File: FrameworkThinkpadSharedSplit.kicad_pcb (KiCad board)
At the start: 2 copper layers, 298.1 x 158.9 mm, 171 parts, among them J1 Conn_01x05_Socket, J10 Conn_01x06_Socket, J11 Conn_01x06_Socket, J12 Conn_01x06_Socket, J2 Conn_01x05_Socket, J3 Conn_01x05_Socket, J4 Conn_01x07_Socket, J5 Conn_01x07_Socket, J6 Conn_01x07_Socket, J7 Conn_01x07_Socket, J8 Conn_01x05_Socket, U1 RP2040_Pro_Micro, U2 Arduino_Pro_Micro

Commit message: added missing row and pullup resistors
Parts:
- removed D36, D37, D38, D39: Diode, ScottoKeebs_Components:Diode_SOD-123
- removed J1, J2, J3, J8: Conn_01x05_Socket, Connector_Molex:Molex_PicoBlade_53048-0510_1x05_P1.25mm_Horizontal
- removed S36, S37, S38, S39: Keyswitch, ScottoKeebs_Choc:Choc_V1V2_1.00u
- added D29: Diode, ScottoKeebs_Components:Diode_SOD-123, B.Cu at (51.0, 179.7)
- added D30: Diode, ScottoKeebs_Components:Diode_SOD-123, B.Cu at (70.0, 179.7)
- added D31: Diode, ScottoKeebs_Components:Diode_SOD-123, B.Cu at (89.0, 179.7)
- added D32: Diode, ScottoKeebs_Components:Diode_SOD-123, B.Cu at (107.0, 179.7)
- added D67: Diode, ScottoKeebs_Components:Diode_SOD-123, B.Cu at (255.0, 162.3)
- added D68: Diode, ScottoKeebs_Components:Diode_SOD-123, B.Cu at (274.0, 162.3)
- added D69: Diode, ScottoKeebs_Components:Diode_SOD-123, B.Cu at (292.0, 162.7)
- added D70: Diode, ScottoKeebs_Components:Diode_SOD-123, B.Cu at (311.0, 162.3)
- added D71: Diode, ScottoKeebs_Components:Diode_SOD-123, B.Cu at (199.0, 179.7)
- added D72: Diode, ScottoKeebs_Components:Diode_SOD-123, B.Cu at (218.0, 179.7)
- added D73: Diode, ScottoKeebs_Components:Diode_SOD-123, B.Cu at (236.0, 179.7)
- added D74: Diode, ScottoKeebs_Components:Diode_SOD-123, B.Cu at (255.0, 179.7)
- added D75: Diode, ScottoKeebs_Components:Diode_SOD-123, B.Cu at (273.0, 179.7)
- added D76: Diode, ScottoKeebs_Components:Diode_SOD-123, B.Cu at (292.0, 179.7)
- added D78: Diode, ScottoKeebs_Components:Diode_SOD-123, B.Cu at (311.0, 179.7)
- added D79: Diode, ScottoKeebs_Components:Diode_SOD-123, B.Cu at (199.0, 197.7)
- added D80: Diode, ScottoKeebs_Components:Diode_SOD-123, B.Cu at (218.0, 197.3)
- added D81: Diode, ScottoKeebs_Components:Diode_SOD-123, B.Cu at (236.0, 197.3)
- added J13: Conn_01x06_Socket, Connector_Molex:Molex_PicoBlade_53048-0610_1x06_P1.25mm_Horizontal, B.Cu at (29.0, 125.0)
- added J14: Conn_01x06_Socket, Connector_Molex:Molex_PicoBlade_53048-0610_1x06_P1.25mm_Horizontal, B.Cu at (167.3, 126.9)
- added J15: Conn_01x06_Socket, Connector_Molex:Molex_PicoBlade_53048-0610_1x06_P1.25mm_Horizontal, B.Cu at (179.0, 133.2)
- added J9: Conn_01x06_Socket, Connector_Molex:Molex_PicoBlade_53048-0610_1x06_P1.25mm_Horizontal, F.Cu at (36.0, 84.3)
- added R6: Resistor 4.7k, ScottoKeebs_Components:Resistor_1206, F.Cu at (36.5, 65.0)
- added R7: Resistor 4.7k, ScottoKeebs_Components:Resistor_1206, F.Cu at (44.0, 65.0)
- added S29: Keyswitch, ScottoKeebs_Choc:Choc_V1V2_1.00u, F.Cu at (43.0, 181.9)
- added S30: Keyswitch, ScottoKeebs_Choc:Choc_V1V2_1.00u, F.Cu at (61.6, 181.9)
- added S31: Keyswitch, ScottoKeebs_Choc:Choc_V1V2_1.00u, F.Cu at (80.2, 181.9)
- added S32: Keyswitch, ScottoKeebs_Choc:Choc_V1V2_1.00u, F.Cu at (98.8, 181.9)
- added S67: Keyswitch, ScottoKeebs_Choc:Choc_V1V2_1.00u, F.Cu at (246.5, 164.3)
- added S68: Keyswitch, ScottoKeebs_Choc:Choc_V1V2_1.00u, F.Cu at (265.1, 164.3)
- added S69: Keyswitch, ScottoKeebs_Choc:Choc_V1V2_1.00u, F.Cu at (283.7, 164.3)
- added S70: Keyswitch, ScottoKeebs_Choc:Choc_V1V2_1.00u, F.Cu at (302.3, 164.3)
- added S71: Keyswitch, ScottoKeebs_Choc:Choc_V1V2_1.00u, F.Cu at (190.7, 181.9)
- added S72: Keyswitch, ScottoKeebs_Choc:Choc_V1V2_1.00u, F.Cu at (209.3, 181.9)
- added S73: Keyswitch, ScottoKeebs_Choc:Choc_V1V2_1.00u, F.Cu at (227.9, 181.9)
- added S74: Keyswitch, ScottoKeebs_Choc:Choc_V1V2_1.00u, F.Cu at (246.5, 181.9)
- added S75: Keyswitch, ScottoKeebs_Choc:Choc_V1V2_1.00u, F.Cu at (265.1, 181.9)
- added S76: Keyswitch, ScottoKeebs_Choc:Choc_V1V2_1.00u, F.Cu at (283.7, 181.9)
- added S77: Keyswitch, ScottoKeebs_Choc:Choc_V1V2_1.00u, F.Cu at (302.3, 181.9)
- added S78: Keyswitch, ScottoKeebs_Choc:Choc_V1V2_1.00u, F.Cu at (190.7, 199.5)
- added S79: Keyswitch, ScottoKeebs_Choc:Choc_V1V2_1.00u, F.Cu at (209.3, 199.5)
- added S80: Keyswitch, ScottoKeebs_Choc:Choc_V1V2_1.00u, F.Cu at (227.9, 199.5)
- moved D40 172.6 mm to (126.0, 197.7)
- moved D42 172.3 mm to (163.0, 197.0)
- moved S40 171.9 mm to (117.5, 199.5)
- moved S41 171.9 mm to (136.1, 199.5)
- moved S42 171.9 mm to (154.7, 199.5)
- moved D41 171.4 mm to (145.0, 197.0)
- moved J4 41.9 mm to (89.2, 84.1)
- moved J6 36.9 mm to (49.5, 84.0)
- moved REF** 23.5 mm to (311.0, 204.0)
- moved REF** 23.5 mm to (34.0, 204.0)
- moved D65 18.6 mm to (218.0, 161.7)
- moved D43 18.2 mm to (199.0, 109.0)
- moved D50 18.2 mm to (199.0, 127.0)
- moved D53 18.2 mm to (255.0, 127.0)
- moved D56 18.2 mm to (311.0, 127.0)
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- renumbered D29 to D82, D30 to D83, D31 to D84, D32 to D85, D67 to D86
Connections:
- S40 pad 1: Net-(J5-Pin_5) -> Net-(J7-Pin_5)
- S41 pad 1: Net-(J5-Pin_6) -> Net-(J7-Pin_6)
- S42 pad 1: Net-(J5-Pin_7) -> Net-(J7-Pin_7)
- U1 pad 10: Col 4 -> Col 10
- U1 pad 11: Col 5 -> Col 11
- U1 pad 12: Col 6 -> Col 12
- U1 pad 13: Col 7 -> Col 13
- U1 pad 14: Col 8 -> Caps Led
- U1 pad 15: Col 9 -> Row 5
- U1 pad 16: Col 10 -> Row 4
- U1 pad 17: Col 11 -> Row 3
- U1 pad 18: Col 12 -> Row 2
- U1 pad 19: Numpad Led -> Row 1
- U1 pad 2: Col 0 -> Trackpoint Data
- U1 pad 20: Caps Led -> Row 0
- U1 pad 21: Row 4 -> Col 1
- U1 pad 22: Row 3 -> Col 2
- U1 pad 23: Row 2 -> Col 3
- U1 pad 24: Row 1 -> Col 4
- U1 pad 25: Row 0 -> Col 5
- U1 pad 26: Col 13 -> Col 6
- U1 pad 29: Trackpoint GND -> unconnected-(U1-GND-Pad29)
- U1 pad 3: Col 1 -> Trackpoint Clock
- U1 pad 30: LED PWR -> unconnected-(U1-5v-Pad30)
- U1 pad 31: unconnected-(U1-GP11-Pad31) -> Col 0
- U1 pad 4: Power LED GND -> Trackpoint GND
- U1 pad 5: unconnected-(U1-GND-Pad5) -> Power LED GND
- U1 pad 6: Col 2 -> Numpad Led
- U1 pad 7: Col 3 -> Col 7
- U1 pad 8: Trackpoint Data -> Col 8
- U1 pad 9: Trackpoint Clock -> Col 9
- U2 pad 21: unconnected-(U2-VCC-Pad21) -> LED PWR
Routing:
- net Net-(D71-K): track 0.00 -> 203.9 mm, vias 0 -> 2
- net Net-(D79-K): track 0.00 -> 136.0 mm, vias 0 -> 2
- net Net-(D40-K): track 159.8 -> 275.1 mm
- net Trackpoint Data: track 0.00 -> 94.3 mm, vias 0 -> 3
- net Trackpoint GND: track 0.00 -> 87.1 mm, vias 0 -> 2
- net Trackpoint Clock: track 0.00 -> 86.2 mm, vias 0 -> 3
- net Net-(D64-K): track 124.9 -> 188.4 mm, vias 0 -> 2
- net Net-(J11-Pin_6): track 0.00 -> 59.5 mm
- net Trackpoint PWR: track 0.00 -> 57.4 mm, vias 0 -> 1
- net Net-(J11-Pin_5): track 0.00 -> 57.4 mm
- net Net-(J11-Pin_4): track 0.00 -> 54.3 mm
- net Col 7: track 75.9 -> 21.7 mm, vias 2 -> 0
- net Row 5: track 0.00 -> 53.5 mm
- net Net-(J11-Pin_3): track 0.00 -> 50.8 mm
- net LED PWR: track 77.1 -> 26.4 mm
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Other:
- board size 298.1 x 158.9 mm -> 298.1 x 174.5 mm

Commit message: shrunk pcb down on the top and bottom
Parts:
- moved J7 26.2 mm to (29.4, 122.5), turned to 90 degrees
- moved J5 24.9 mm to (179.0, 122.3), turned to 90 degrees
- moved J12 9.60 mm to (257.7, 92.9)
- moved J4 9.60 mm to (89.2, 93.7)
- moved J9 9.60 mm to (36.0, 93.9)
- moved R1 9.60 mm to (276.8, 92.6)
- moved R2 9.60 mm to (285.3, 96.1)
- moved R3 9.60 mm to (293.1, 92.6)
- moved R4 9.60 mm to (300.8, 96.1)
- moved R5 9.60 mm to (309.8, 93.1)
- moved REF** 9.60 mm to (316.8, 93.1)
- moved REF** 9.60 mm to (243.8, 93.1)
- moved J10 9.60 mm to (106.1, 64.5)
- moved J11 9.60 mm to (88.9, 52.9)
- moved REF** 9.60 mm to (28.5, 50.9)
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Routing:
- net Net-(J7-Pin_7): track 206.2 -> 235.6 mm
- net Net-(J7-Pin_6): track 188.9 -> 217.9 mm
- net Net-(J7-Pin_5): track 172.0 -> 199.9 mm
- net Net-(J7-Pin_4): track 135.1 -> 161.8 mm
- net Net-(J7-Pin_3): track 118.2 -> 144.8 mm
- net Net-(J7-Pin_2): track 101.4 -> 126.9 mm
- net Net-(J5-Pin_6): track 170.5 -> 195.7 mm
- net Net-(J5-Pin_2): track 122.0 -> 147.0 mm
- net Net-(J5-Pin_5): track 153.0 -> 177.8 mm
- net Net-(J5-Pin_4): track 136.0 -> 160.5 mm
- net Net-(J5-Pin_7): track 187.2 -> 211.4 mm
- net Net-(J5-Pin_3): track 138.8 -> 162.0 mm
- net Net-(J7-Pin_1): track 85.3 -> 108.4 mm
- net Net-(J5-Pin_1): track 105.4 -> 127.3 mm
- net Net-(D29-K): track 260.8 -> 252.1 mm
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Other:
- board size 298.1 x 174.5 mm -> 298.1 x 162.7 mm

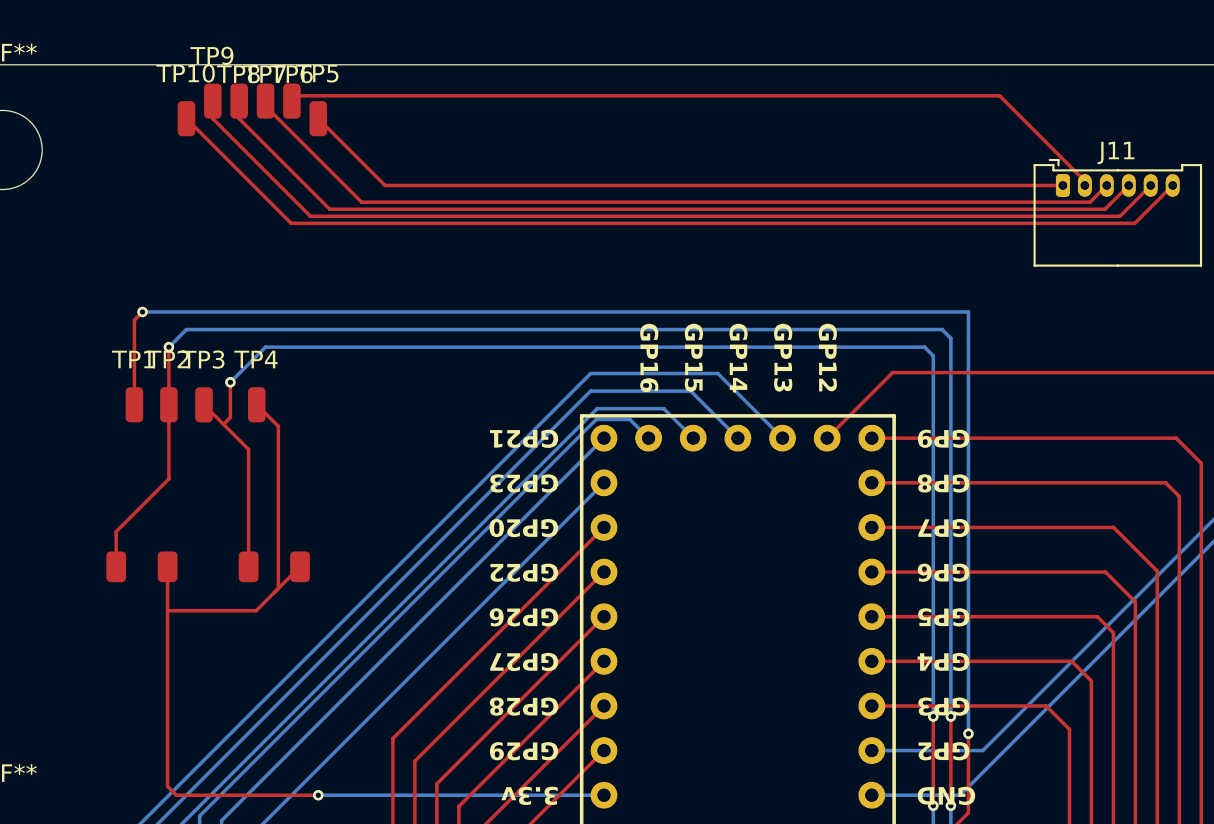
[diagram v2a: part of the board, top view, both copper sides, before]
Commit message: adjusted positioning of trackpoint board
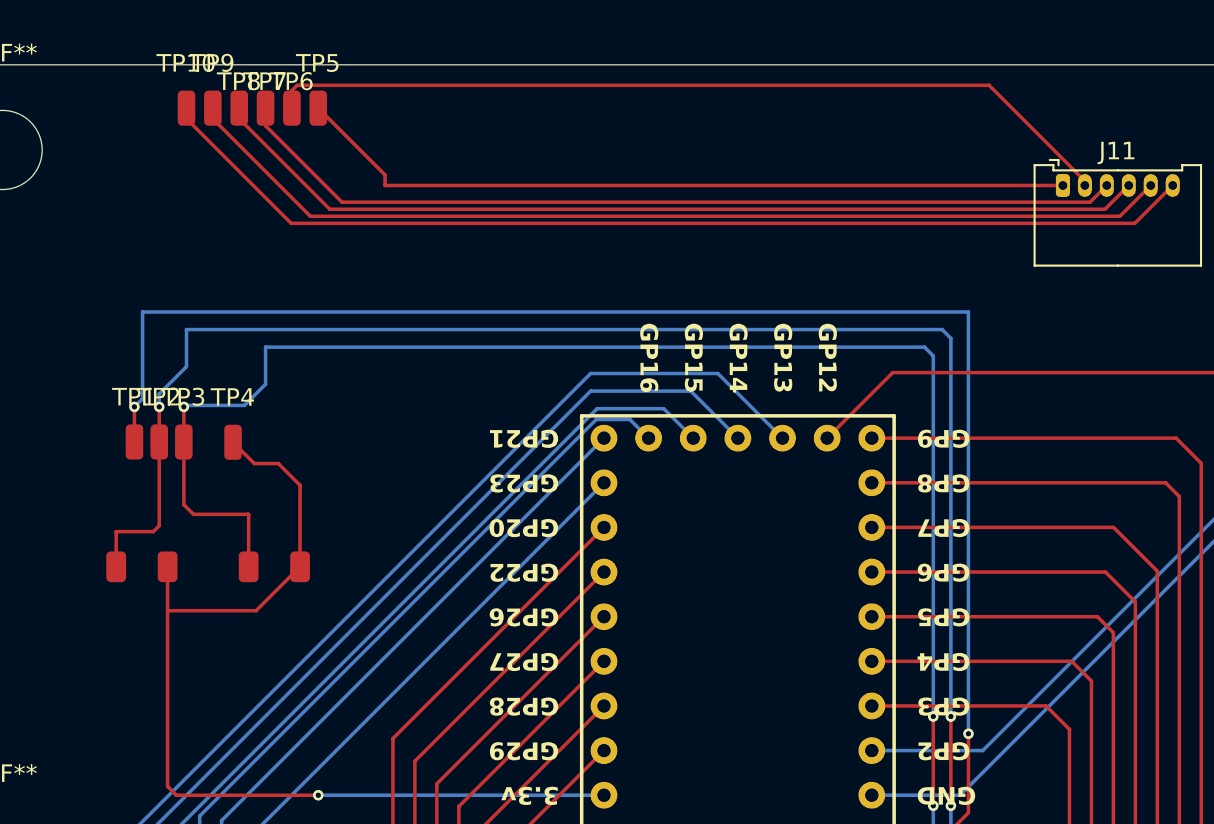
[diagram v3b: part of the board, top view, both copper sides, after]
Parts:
- moved TP4 2.53 mm to (41.6, 67.5)
- moved TP3 2.41 mm to (38.9, 67.5)
- moved TP2 2.18 mm to (37.5, 67.5)
- moved TP1 2.11 mm to (36.0, 67.5)
- moved TP10 0.60 mm to (39.0, 48.5)
- moved TP5 0.60 mm to (46.5, 48.5)
- moved TP6 0.40 mm to (45.0, 48.5)
- moved TP7 0.40 mm to (43.5, 48.5)
- moved TP8 0.40 mm to (42.0, 48.5)
- moved TP9 0.40 mm to (40.5, 48.5)
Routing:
- net Trackpoint Clock: track 86.2 -> 90.3 mm
- net Trackpoint GND: track 87.1 -> 89.2 mm
- net Trackpoint PWR: track 57.4 -> 55.6 mm
- net Net-(J11-Pin_2): track 47.5 -> 49.2 mm
- net Trackpoint Data: track 94.3 -> 95.6 mm
- net Net-(J11-Pin_6): track 59.5 -> 60.1 mm
- net Net-(J11-Pin_1): track 43.9 -> 44.5 mm
